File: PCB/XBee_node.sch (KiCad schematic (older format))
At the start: 20 parts, among them J1 conn_2x16, U1 Nano, U2 MCP2515, U3 MCP2551, U4 PushButton, U5 XBee_adapter, U6 DIPSwitch_12, U7 DIPSwitch_3, Y1 16MHz

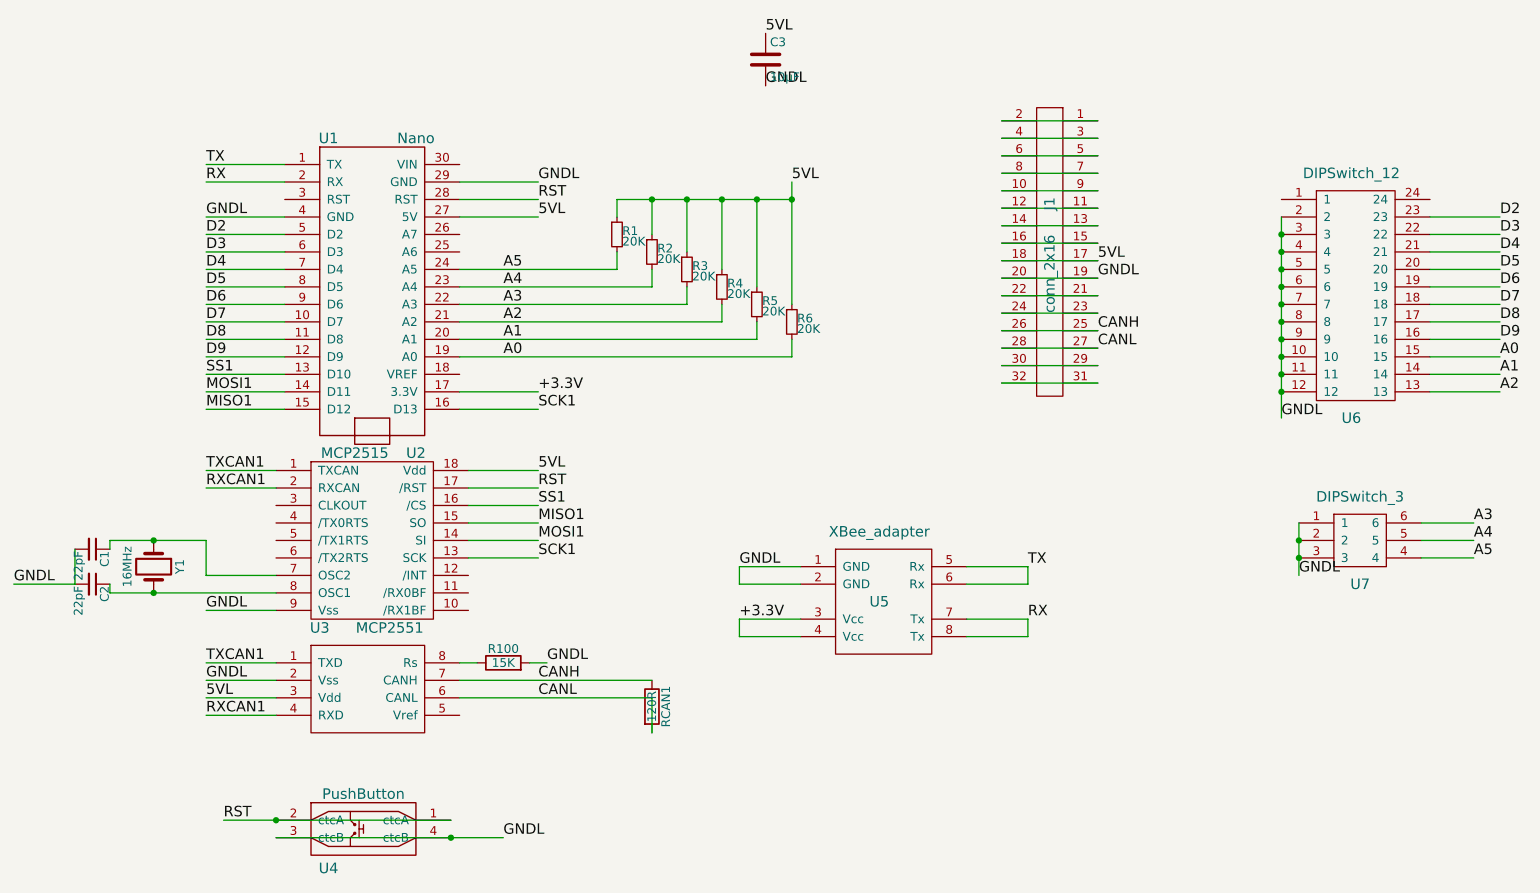
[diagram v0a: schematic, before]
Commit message: reduced ID to implement SoftwareSerial
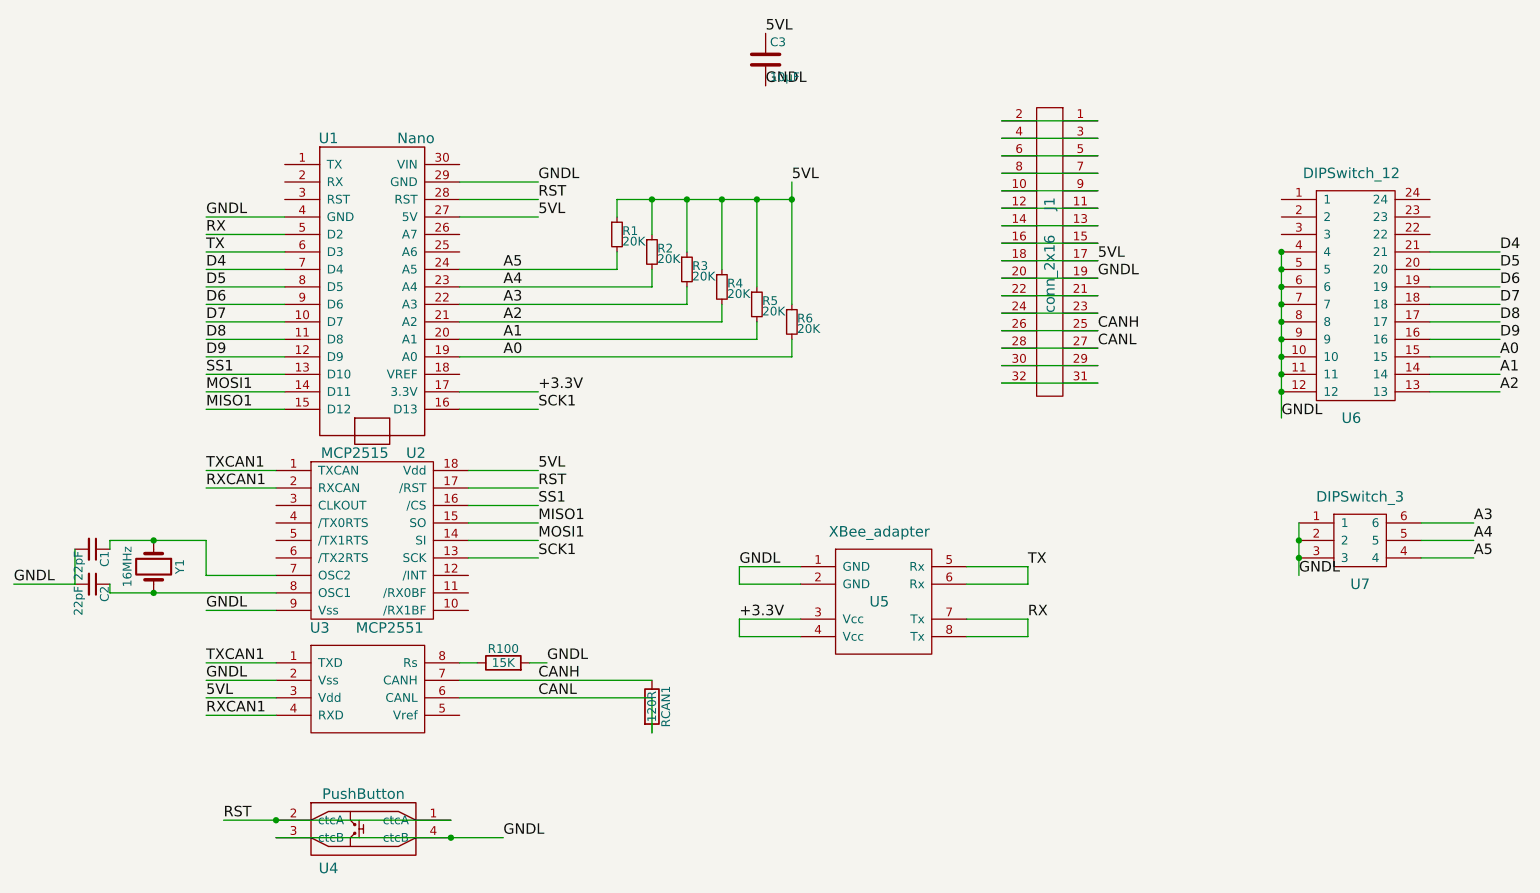
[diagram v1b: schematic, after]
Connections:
- net GNDL: no longer U6.2, U6.3
- net RX: now also U1.5 (D2); no longer U1.2 (RX)
- net TX: now also U1.6 (D3); no longer U1.1 (TX)
- net D2: no longer names the net of U6.23
- net D2: no longer U1.5 (D2)
- net D3: no longer names the net of U6.22
- net D3: no longer U1.6 (D3)
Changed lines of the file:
@@
 LIBS:contrib
 LIBS:valves
-LIBS:Libabar
 LIBS:XBee_node-cache
 EELAYER 25 0
@@
 Text Label 5400 4150 0    60   ~ 0
 +3.3V
-Text Label 2350 1550 0    60   ~ 0
-TX
-Text Label 2350 1650 0    60   ~ 0
-RX
 Text Label 7050 3850 0    60   ~ 0
 TX
@@
 	5400 4250 5400 4150
 Wire Wire Line
-	2800 1550 2350 1550
-Wire Wire Line
-	2800 1650 2350 1650
-Wire Wire Line
 	3800 2850 4250 2850
-Connection ~ 8500 1950
 Connection ~ 8500 2050
 Connection ~ 8500 2150
@@
 Connection ~ 8500 2850
 Wire Wire Line
-	8500 1850 8500 3000
-Wire Wire Line
 	2350 1950 2800 1950
 Wire Wire Line
@@
 Text Label 2350 1850 0    60   ~ 0
 GNDL
-Text Label 2350 1950 0    60   ~ 0
-D2
-Text Label 2350 2050 0    60   ~ 0
-D3
 Text Label 2350 2150 0    60   ~ 0
 D4
@@
 D9
 Wire Wire Line
-	9350 1850 9750 1850
-Wire Wire Line
-	9350 1950 9750 1950
-Wire Wire Line
 	9350 2050 9750 2050
 Wire Wire Line
@@
 Wire Wire Line
 	9350 2550 9750 2550
-Text Label 9750 1850 0    60   ~ 0
-D2
-Text Label 9750 1950 0    60   ~ 0
-D3
 Text Label 9750 2050 0    60   ~ 0
 D4
@@
 Text Label 5550 1100 0    60   ~ 0
 GNDL
+Wire Wire Line
+	8500 2050 8500 3000
+Text Label 2350 2050 0    60   ~ 0
+TX
+Text Label 2350 1950 0    60   ~ 0
+RX
 $EndSCHEMATC
